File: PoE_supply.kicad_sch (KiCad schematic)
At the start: 38 parts, among them J1 Bus_RJ45_5-2337992-8, Q1 PJE138K, Q2 PJE138K, Q3 PJE138K, U1 TPS2372-3RGWR, U4 IEA48003A280V-001-R

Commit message: [#63274] Add testpoints, improve silcscreen
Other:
- company: Antmicro ltd. -> Antmicro
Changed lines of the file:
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@@
     (title "PoE to USBC PD adapter")
     (date "2024-07-08")
-    (company "Antmicro ltd.")
+    (rev "1.0.0")
+    (company "Antmicro")
   )
   (bus_alias "MDI" (members "MDI0_P" "MDI0_N" "MDI1_P" "MDI1_N" "MDI2_P" "MDI2_N" "MDI3_N" "MDI3_P"))

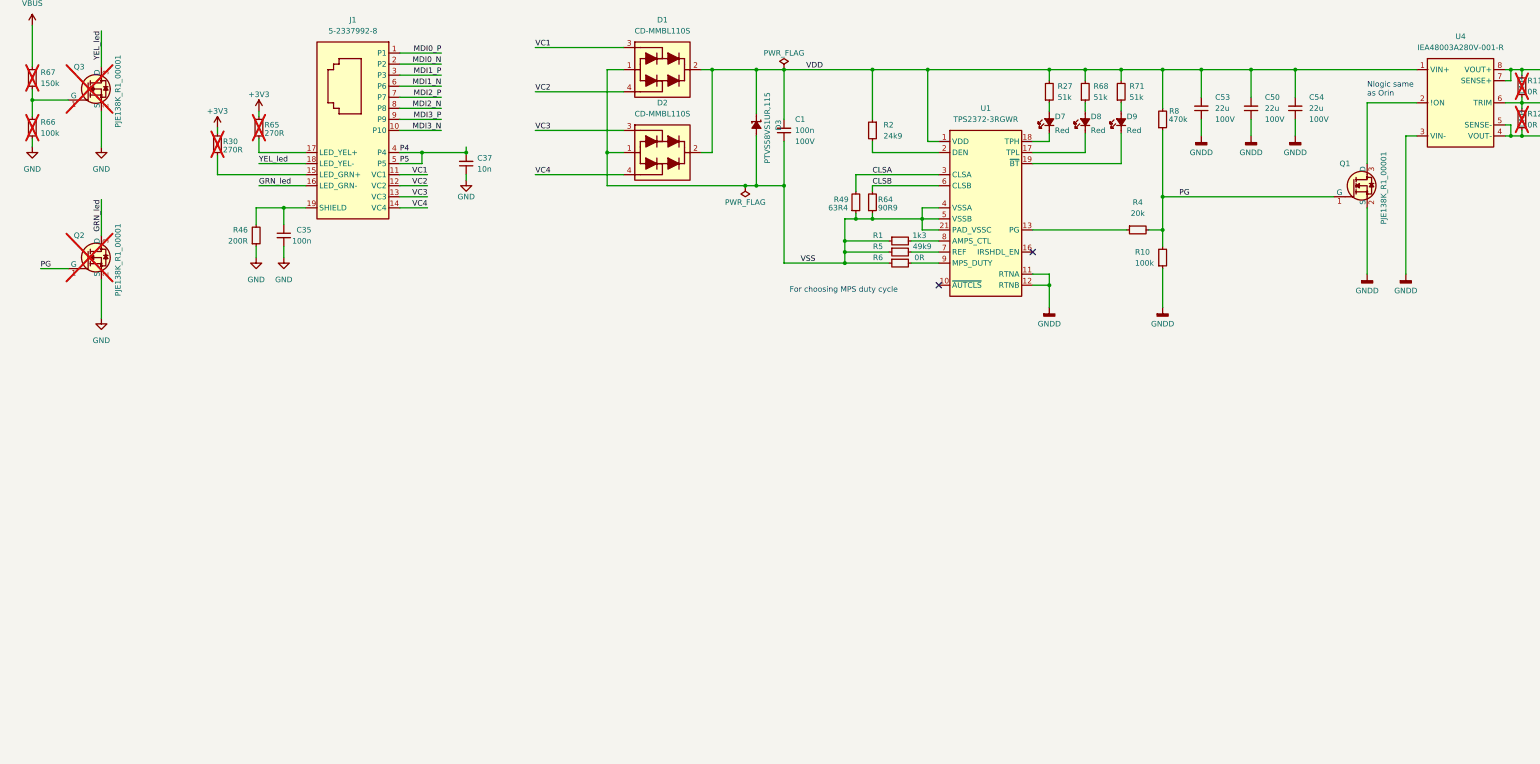
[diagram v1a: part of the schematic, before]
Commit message: [#63274] Add optocouplers for ETH diode, TPS65987D HRESET
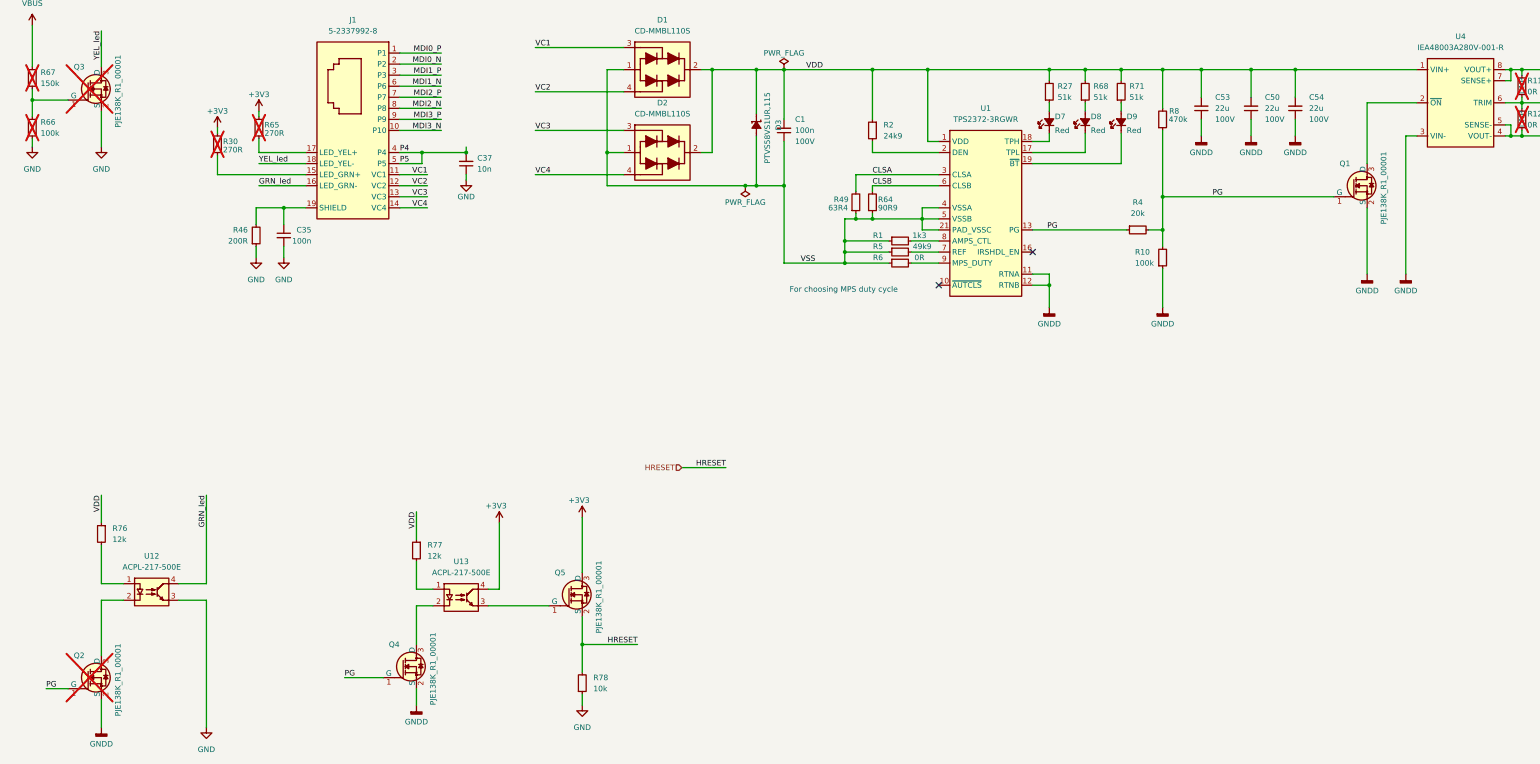
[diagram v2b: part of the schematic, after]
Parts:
- added Q4, Q5: PJE138K, antmicro-footprints:SOT-523, symbol antmicroTransistorsFETsMOSFETsSingle:PJE138K
- added R76, R77: R_12k_2010, antmicro-footprints:R_2010_5025Metric, symbol antmicroResistorsmisc:R_12k_2010
- added R78: R_10k_0402, antmicro-footprints:R_0402_1005Metric, symbol antmicroResistors0402:R_10k_0402
- added U12, U13: ACPL-217-500E, antmicro-footprints:SOIC-4_4.55x2.6mm_P1.27mm, symbol antmicroOptoisolatorsLogicOutput:ACPL-217-500E
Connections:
- net +3V3: now also Q5.3 (D), U13.4
- net GND: now also R78.1, U12.3; no longer Q2.2 (S)
- net GNDD: now also Q2.2 (S), Q4.2 (S)
- net GRN_led: now also U12.4; no longer Q2.3 (D)
- net PG: now also R4.1, U1.13 (PG), Q4.1 (G)
- net VDD: now also R76.1, R77.1
- new net: Q4.3 (D), U13.2
- new net: Q2.3 (D), U12.2
- new net: R77.2, U13.1
- new net: R76.2, U12.1
- new net: Q5.1 (G), U13.3
- new net HRESET: Q5.2 (S), R78.2
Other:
- note removed: "Nlogic same as Orin"
- moved on the sheet: Q2

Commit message: [#63274] Remove one optocoupler, add components to PCB, route PCB
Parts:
- removed Q2: PJE138K, antmicro-footprints:SOT-523, symbol antmicroTransistorsFETsMOSFETsSingle:PJE138K
- removed R76: R_12k_2010, antmicro-footprints:R_2010_5025Metric, symbol antmicroResistorsmisc:R_12k_2010
- removed R78: R_10k_0402, antmicro-footprints:R_0402_1005Metric, symbol antmicroResistors0402:R_10k_0402
- removed U12: ACPL-217-500E, antmicro-footprints:SOIC-4_4.55x2.6mm_P1.27mm, symbol antmicroOptoisolatorsLogicOutput:ACPL-217-500E
- added R79: R_100k_0402, antmicro-footprints:R_0402_1005Metric, symbol antmicroResistors0402:R_100k_0402
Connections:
- net +3V3: now also R79.2; no longer U13.4
- net GND: now also U13.3
- net GRN_led: now also Q5.1 (G), U13.4, R79.1
- net PG: no longer Q1.1 (G), Q4.1 (G), R10.2, R4.2, R8.1
- new net: Q1.1 (G), Q4.1 (G), R10.2, R4.2, R8.1
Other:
- moved on the sheet: C1, C2, C35, C37, C50, C53, C54, D1, D2, D3, D7, D8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

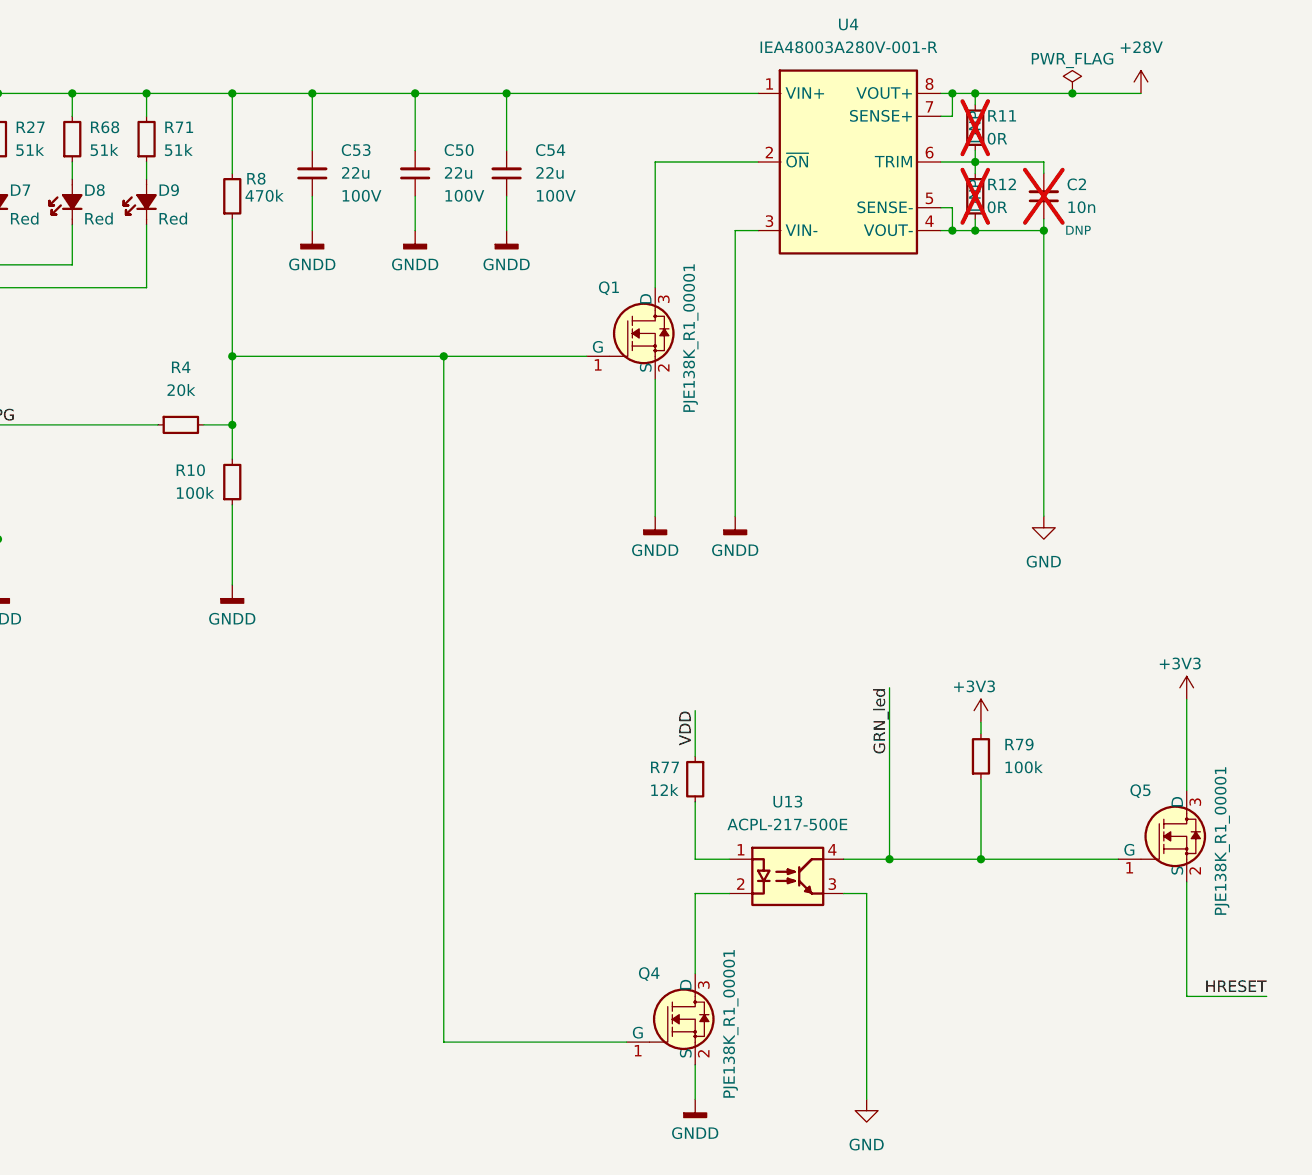
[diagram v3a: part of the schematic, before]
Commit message: [#63274] Change transistors to BS5123
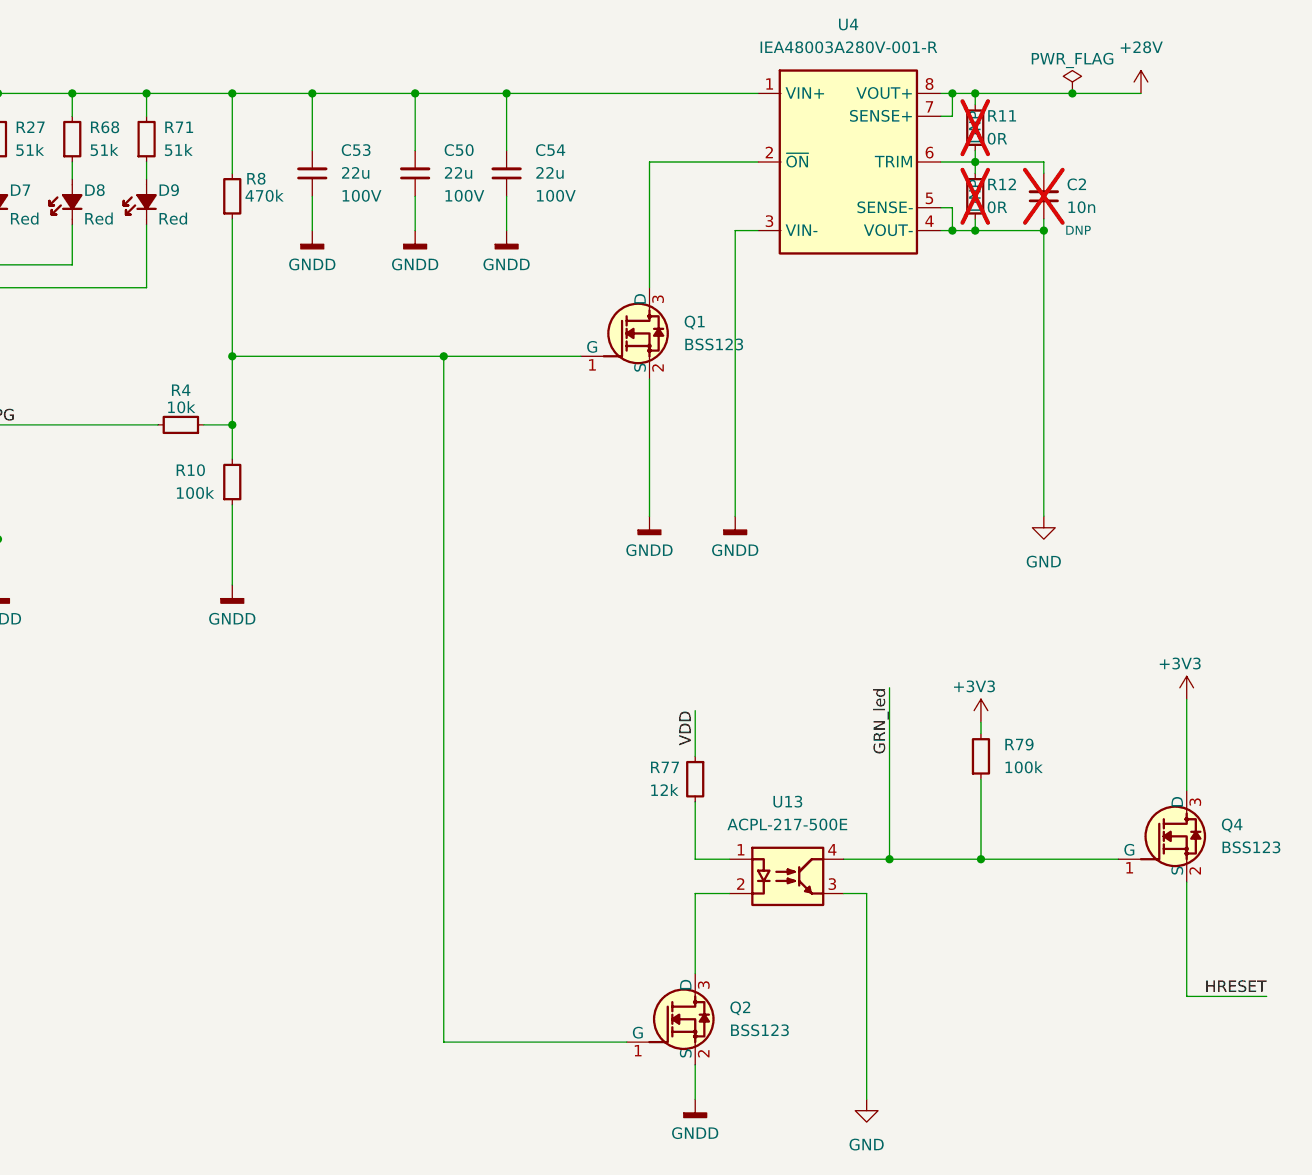
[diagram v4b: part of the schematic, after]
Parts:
- removed Q1, Q4, Q5: PJE138K, antmicro-footprints:SOT-523, symbol antmicroTransistorsFETsMOSFETsSingle:PJE138K
- removed R4: R_20k_0402, antmicro-footprints:R_0402_1005Metric, symbol antmicroResistors0402:R_20k_0402
- added Q1, Q2, Q4: BSS123, antmicro-footprints:SOT-23-3, symbol antmicroTransistorsFETsMOSFETsSingle:BSS123
- added R4: R_10k_0402, antmicro-footprints:R_0402_1005Metric, symbol antmicroResistors0402:R_10k_0402
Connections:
- net +3V3: now also Q4.3 (D)
- net GNDD: now also Q1.2 (S), Q2.2 (S)
- net GRN_led: now also Q4.1 (G)
- net HRESET: now also Q4.2 (S)
- net PG: now also R4.2
- net at R10.2, R8.1: now also Q1.1 (G), Q2.1 (G), R4.1
- net at U13.2: now also Q2.3 (D)
- net at U4.2 (~{ON}): now also Q1.3 (D)

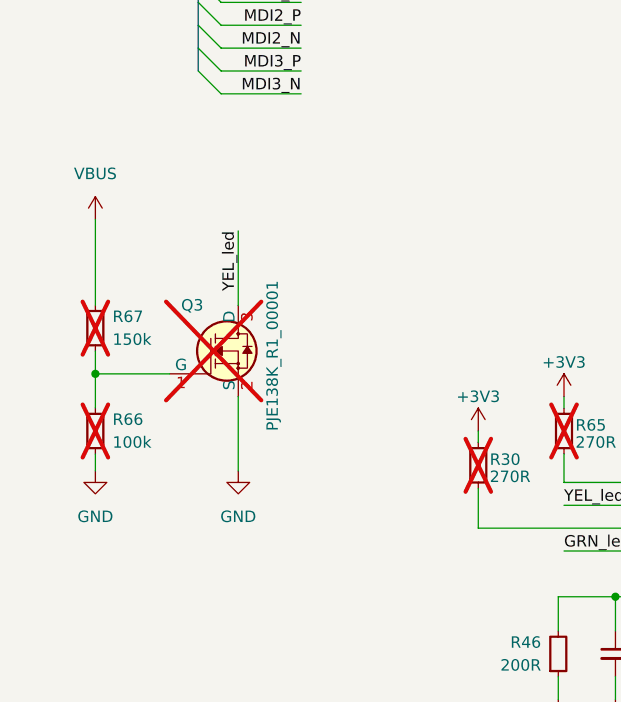
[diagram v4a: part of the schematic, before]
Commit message: [#63274] Placed transistors on PCB, routed, cleared DRC
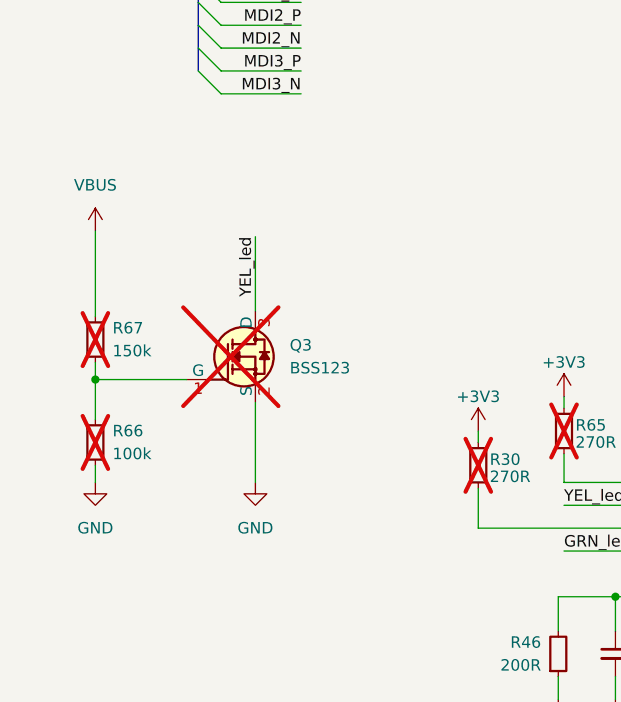
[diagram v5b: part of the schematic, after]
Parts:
- removed Q3: PJE138K, antmicro-footprints:SOT-523, symbol antmicroTransistorsFETsMOSFETsSingle:PJE138K
- added Q3: BSS123, antmicro-footprints:SOT-23-3, symbol antmicroTransistorsFETsMOSFETsSingle:BSS123
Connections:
- net GND: now also Q3.2 (S)
- net YEL_led: now also Q3.3 (D)
- net at R66.2, R67.1: now also Q3.1 (G)
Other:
- moved on the sheet: R66, R67
